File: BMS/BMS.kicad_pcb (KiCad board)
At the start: 2 copper layers, 53 parts, among them J1 Cell Taps, Q1 NSV1C201MZ4, Q2 BSS308PE, Q3 BSS308PE, Q4 BSS308PE, Q5 BSS308PE, Q6 BSS308PE, Q7 BSS308PE, Q8 BSS308PE, SW1 SW_DIP_x04, U1 LTC6811

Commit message: Updated BMS
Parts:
- added C12: 15pF, Capacitors_SMD:C_0805_HandSoldering, F.Cu at (390.8, 287.8)
- added C13: 1uF, Capacitors_SMD:C_0805_HandSoldering, F.Cu at (395.3, 287.8)
- added C14: 1uF, Capacitors_SMD:C_0805_HandSoldering, F.Cu at (390.8, 289.6)
- added J10: Current Sensor, Connectors_Molex:Molex_NanoFit_1x03x2.50mm_Straight, F.Cu at (368.5, 274.3)
- added J2: IsoSPI, Connectors_Molex:Molex_NanoFit_1x02x2.50mm_Straight, F.Cu at (368.5, 281.6)
- added J3: Temp 1, Connectors_Molex:Molex_NanoFit_1x02x2.50mm_Straight, F.Cu at (378.7, 274.3)
- added J4: Temp 2, Connectors_Molex:Molex_NanoFit_1x02x2.50mm_Straight, F.Cu at (368.5, 289.0)
- added J5: Temp 3, Connectors_Molex:Molex_NanoFit_1x02x2.50mm_Straight, F.Cu at (376.1, 281.6)
- added J6: Temp 4, Connectors_Molex:Molex_NanoFit_1x02x2.50mm_Straight, F.Cu at (386.3, 274.3)
- added J7: Temp 5, Connectors_Molex:Molex_NanoFit_1x02x2.50mm_Straight, F.Cu at (376.1, 289.0)
- added J8: Temp 6, Connectors_Molex:Molex_NanoFit_1x02x2.50mm_Straight, F.Cu at (383.8, 281.6)
- added J9: Temp 7, Connectors_Molex:Molex_NanoFit_1x02x2.50mm_Straight, F.Cu at (383.8, 289.0)
- added L1: HM2113ZNL, FSFootprints:HM2113ZNL, F.Cu at (361.1, 280.1)
- added R32: 402, Resistors_SMD:R_0805_HandSoldering, F.Cu at (358.9, 291.0)
- added R33: R, Resistors_SMD:R_0805_HandSoldering, F.Cu at (358.9, 292.9)
- added R34: R, Resistors_SMD:R_0805_HandSoldering, F.Cu at (393.4, 272.9)
- added R35: R, Resistors_SMD:R_0805_HandSoldering, F.Cu at (393.4, 274.8)
- added R36: R, Resistors_SMD:R_0805_HandSoldering, F.Cu at (393.4, 276.7)
- added R37: R, Resistors_SMD:R_0805_HandSoldering, F.Cu at (390.9, 280.3)
- added R38: R, Resistors_SMD:R_0805_HandSoldering, F.Cu at (390.9, 282.2)
- added R39: R, Resistors_SMD:R_0805_HandSoldering, F.Cu at (390.9, 284.1)
- added R40: 22, Resistors_SMD:R_0805_HandSoldering, F.Cu at (390.9, 286.0)
- added R41: 22, Resistors_SMD:R_0805_HandSoldering, F.Cu at (358.9, 289.1)
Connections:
- net Net-(R12-Pad1) renamed ICMP
- net Net-(R12-Pad2) renamed IBIAS
- U1 pad 32: (no net) -> Net-(J10-Pad2)
- U1 pad 41: (no net) -> IMA
- U1 pad 42: (no net) -> IPA

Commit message: Begin work on BMS schematic
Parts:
- C1, C11, C13, C14, C3, Q1, R12, R17, R2, R5, R6, R7, R8: moved to B.Cu
- J1: value Cell Taps -> Molex_Nano-Fit_105309-xx08_1x08_P2.50mm_Vertical; footprint FSFootprints:Cell Taps -> Connector_Molex:Molex_Nano-Fit_105309-xx08_1x08_P2.50mm_Vertical
- moved R30 244.7 mm to (273.9, 305.0), turned to 0 degrees
- moved Q8 227.4 mm to (283.5, 305.0), turned to 180 degrees
- moved R31 207.4 mm to (322.1, 292.1), turned to 0 degrees
- moved Q2 200.6 mm to (283.5, 275.0), turned to 180 degrees
- moved C6 184.7 mm to (347.8, 288.5), turned to 180 degrees
- moved R9 182.6 mm to (273.9, 275.0), turned to 0 degrees
- moved R27 181.2 mm to (273.9, 300.0), turned to 0 degrees
- moved Q3 168.7 mm to (283.5, 280.0), turned to 180 degrees
- moved Q7 165.2 mm to (283.5, 300.0), turned to 180 degrees
- moved R14 151.8 mm to (273.9, 280.0), turned to 0 degrees
- moved Q4 130.1 mm to (283.5, 285.0), turned to 180 degrees
- moved R24 124.9 mm to (273.9, 295.0), turned to 0 degrees
- moved R23 115.5 mm to (289.9, 296.0)
- moved Q6 113.2 mm to (283.5, 295.0), turned to 180 degrees
- moved J10 111.0 mm to (261.5, 303.8), turned to 270 degrees
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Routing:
- net V-: track 0.00 -> 57.8 mm
- net Net-(J1-Pad1): track 0.00 -> 40.6 mm
- net Net-(J1-Pad2): track 0.00 -> 32.9 mm
- net Net-(J1-Pad7): track 0.00 -> 31.8 mm
- net Net-(J1-Pad3): track 0.00 -> 31.8 mm
- net Net-(J1-Pad6): track 0.00 -> 30.8 mm
- net Net-(J1-Pad4): track 0.00 -> 30.6 mm
- net Net-(R29-Pad1): track 0.00 -> 30.1 mm
- net Net-(J1-Pad5): track 0.00 -> 29.8 mm
- net Net-(C2-Pad1): track 0.00 -> 25.7 mm
- net Net-(C10-Pad2): track 0.00 -> 24.0 mm, vias 0 -> 1
- net Net-(C5-Pad2): track 0.00 -> 23.9 mm
- net Net-(C2-Pad2): track 0.00 -> 21.3 mm
- net Net-(C10-Pad1): track 0.00 -> 20.3 mm
- net Net-(C4-Pad2): track 0.00 -> 19.5 mm
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
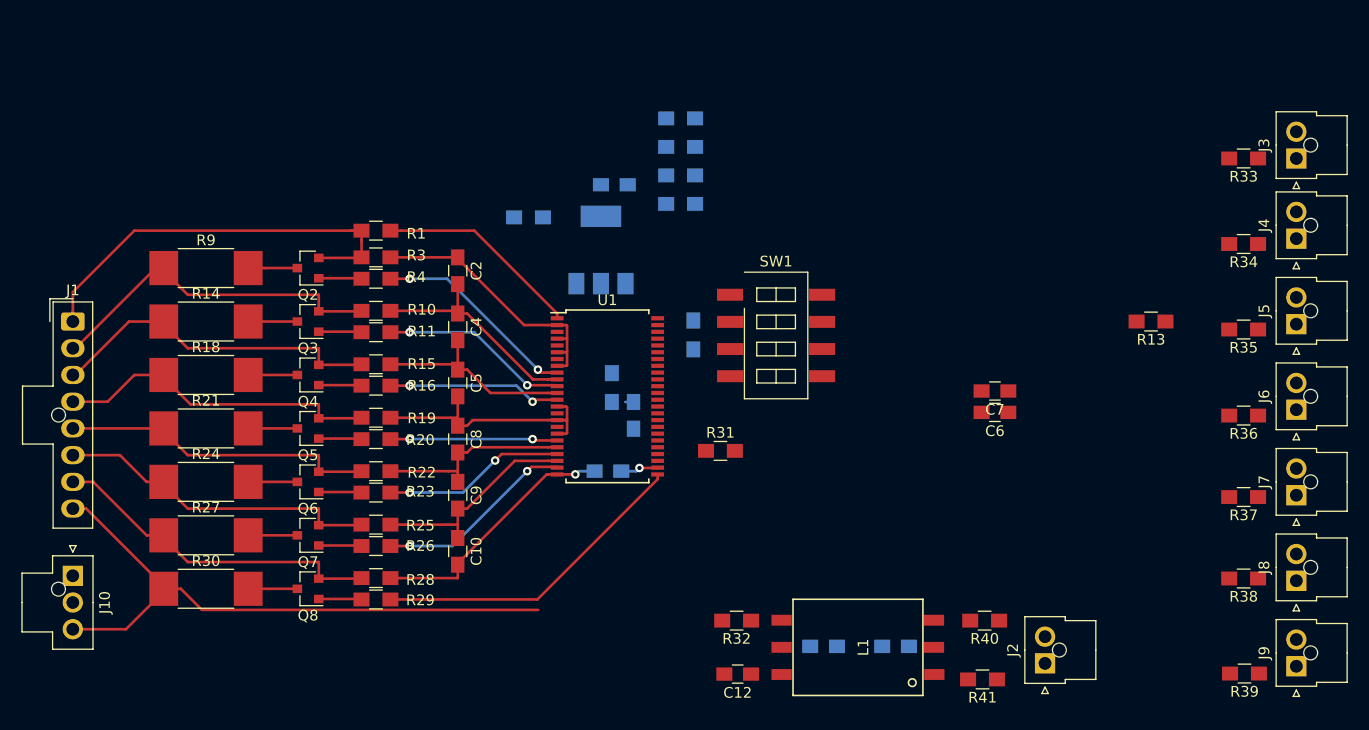
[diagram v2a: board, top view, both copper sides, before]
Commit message: BMS board v0.1
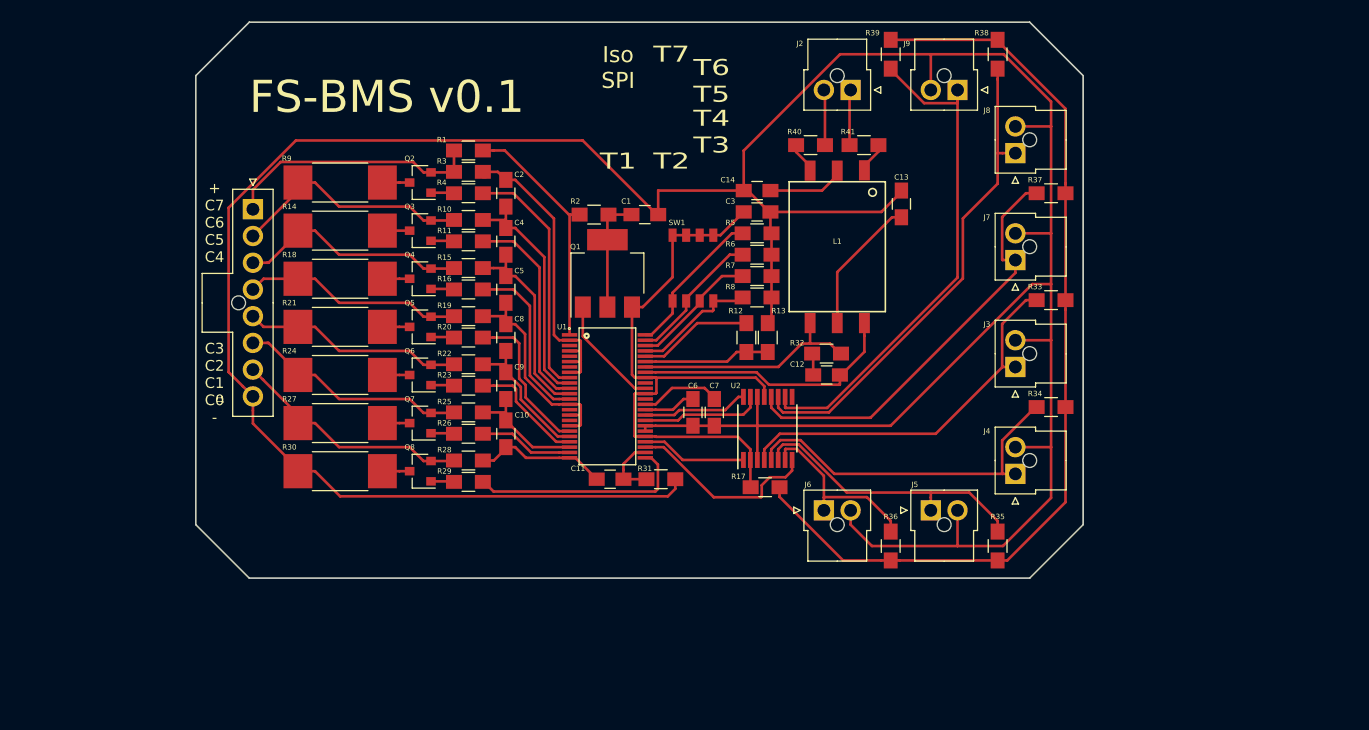
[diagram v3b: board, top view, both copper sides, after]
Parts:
- removed J10: Current Sensor, Connectors_Molex:Molex_NanoFit_1x03x2.50mm_Straight
- added U2: ADG708, Housings_SSOP:TSSOP-16_4.4x5mm_Pitch0.65mm, F.Cu at (326.5, 290.0)
- C1, C11, C3, Q1, R12, R2, R5, R6, R7, R8: moved to F.Cu
- C13, C14: value 1uF -> 10nF; moved to F.Cu
- J1: value Molex_Nano-Fit_105309-xx08_1x08_P2.50mm_Vertical -> Cell Taps; footprint Connector_Molex:Molex_Nano-Fit_105309-xx08_1x08_P2.50mm_Vertical -> Connectors_Molex:Molex_NanoFit_1x08x2.50mm_Straight
- R17: value 1M -> 0; moved to F.Cu
- R33, R34, R35, R36, R37, R38, R39: value R -> 10k
- SW1: footprint Buttons_Switches_SMD:SW_DIP_x4_W8.61mm_Slide_LowProfile -> FSFootprints:DIP A6H-4101
- U1: footprint Housings_SSOP:SSOP-48_7.5x15.9mm_Pitch0.635mm -> FSFootprints:FSOP-48_[LTC6811-2]
- moved R39 66.7 mm to (338.0, 255.0), turned to 90 degrees
- moved J9 62.5 mm to (344.2, 258.3), turned to 180 degrees
- moved J2 56.6 mm to (334.2, 258.3), turned to 180 degrees
- moved R38 54.2 mm to (348.0, 255.0), turned to 90 degrees
- moved R41 51.2 mm to (335.5, 263.5), turned to 0 degrees
- moved J8 47.9 mm to (349.7, 264.2)
- moved R40 47.4 mm to (330.5, 263.5)
- moved J6 45.2 mm to (331.8, 297.7), turned to 0 degrees
- moved C14 44.6 mm to (325.5, 267.8), turned to 180 degrees
- moved C13 42.0 mm to (339.0, 269.0), turned to 90 degrees
- moved J5 38.4 mm to (341.8, 297.7), turned to 0 degrees
- moved L1 37.5 mm to (333.0, 273.0), turned to 180 degrees
- moved R13 35.9 mm to (326.5, 281.5), turned to 270 degrees
- moved R36 35.2 mm to (338.0, 301.0), turned to 270 degrees
- moved J4 34.3 mm to (349.7, 294.2)
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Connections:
- R17 pad 2: Net-(R17-Pad2) -> VREG
- U1 pad 27: (no net) -> TEMP
- U1 pad 28: (no net) -> MUX_A0
- U1 pad 29: (no net) -> VREG
- U1 pad 32: Net-(J10-Pad2) -> MUX_A2
- U1 pad 33: (no net) -> MUX_A1
- U1 pad 39: Net-(R17-Pad2) -> (no net)
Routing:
- net V-: track 57.8 -> 315.6 mm
- net VREG: track 0.51 -> 148.2 mm
- net Net-(J9-Pad1): track 0.00 -> 48.6 mm
- net Net-(J8-Pad1): track 0.00 -> 46.3 mm
- net Net-(J7-Pad1): track 0.00 -> 40.4 mm
- net Net-(J3-Pad1): track 0.00 -> 35.9 mm
- net Net-(J4-Pad1): track 0.00 -> 33.2 mm
- net Net-(J5-Pad1): track 0.00 -> 27.3 mm
- net IMA: track 0.00 -> 25.5 mm
- net IPA: track 0.00 -> 21.5 mm
- net TEMP: track 0.00 -> 18.3 mm
- net Net-(J6-Pad1): track 0.00 -> 17.1 mm
- net Net-(J1-Pad1): track 40.6 -> 24.1 mm
- net A3: track 0.00 -> 14.2 mm
- net A2: track 0.00 -> 13.1 mm
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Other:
- board outline added: 83 x 52 mm
- net class Default: clearance 0.2 -> 0.16
- rule trace_clearance: 0.2 -> 0.16
- board text added: "+ C7 C6 C5 C4"
- board text added: "C3 C2 C1 C0 -"
- board text added: "FS-BMS v0.1"
- board text added: "Iso SPI"
- board text added: "T1"
- board text added: "T2"
- board text added: "T3"
- board text added: "T4"
- board text added: "T5"
- board text added: "T6"
- board text added: "T7"

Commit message: yikes
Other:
- net class Default: clearance 0.16 -> 0.1778
- rule trace_clearance: 0.16 -> 0.1778
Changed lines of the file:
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@@
     (34 B.Paste user hide)
     (35 F.Paste user hide)
-    (36 B.SilkS user)
+    (36 B.SilkS user hide)
     (37 F.SilkS user)
     (38 B.Mask user)
-    (39 F.Mask user)
+    (39 F.Mask user hide)
     (40 Dwgs.User user)
     (41 Cmts.User user)
@@
   (setup
     (last_trace_width 0.25)
-    (trace_clearance 0.16)
+    (trace_clearance 0.1778)
     (zone_clearance 0.508)
     (zone_45_only no)
@@
   (net 69 MUX_A0)
   (net_class Default "This is the default net class."
-    (clearance 0.16)
+    (clearance 0.1778)
     (trace_width 0.25)
     (via_dia 0.8)

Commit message: Began BMS slave board
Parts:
- removed C14: 10nF, Capacitors_SMD:C_0805_HandSoldering
- added D1: LH R974-LP-1, LEDs:LED_0805_HandSoldering, F.Cu at (107.2, 206.5)
- added D2: LH R974-LP-1, LEDs:LED_0805_HandSoldering, F.Cu at (367.2, 266.4)
- added D3: LH R974-LP-1, LEDs:LED_0805_HandSoldering, F.Cu at (372.9, 263.5)
- added D4: LH R974-LP-1, LEDs:LED_0805_HandSoldering, F.Cu at (367.2, 269.2)
- added D5: LH R974-LP-1, LEDs:LED_0805_HandSoldering, F.Cu at (372.9, 266.4)
- added D6: LH R974-LP-1, LEDs:LED_0805_HandSoldering, F.Cu at (367.2, 272.1)
- added D7: LH R974-LP-1, LEDs:LED_0805_HandSoldering, F.Cu at (378.7, 263.5)
- added D8: LH R974-LP-1, LEDs:LED_0805_HandSoldering, F.Cu at (367.2, 274.9)
- added D9: LH R974-LP-1, LEDs:LED_0805_HandSoldering, F.Cu at (321.0, 218.5)
- added R42: 120, Resistors_SMD:R_0805_HandSoldering, F.Cu at (342.5, 204.5)
- added R43: 2.2k, Resistors_SMD:R_0805_HandSoldering, F.Cu at (390.2, 263.5)
- added R44: 2.2k, Resistors_SMD:R_0805_HandSoldering, F.Cu at (378.7, 275.0)
- added R45: 2.2k, Resistors_SMD:R_0805_HandSoldering, F.Cu at (384.4, 269.3)
- added R46: 2.2k, Resistors_SMD:R_0805_HandSoldering, F.Cu at (390.2, 266.4)
- added R47: 2.2k, Resistors_SMD:R_0805_HandSoldering, F.Cu at (378.7, 277.9)
- added R48: 2.2k, Resistors_SMD:R_0805_HandSoldering, F.Cu at (384.4, 272.2)
- added R49: 120, Resistors_SMD:R_0805_HandSoldering, F.Cu at (390.2, 269.3)
- added R50: 120, Resistors_SMD:R_0805_HandSoldering, F.Cu at (384.4, 275.0)
- added R51: 160, Resistors_SMD:R_0805_HandSoldering, F.Cu at (321.0, 221.4)
- J1: footprint Connectors_Molex:Molex_NanoFit_1x08x2.50mm_Straight -> FSFootprints:Cell Taps
- R12: value R -> 1.5k
- R13: value R -> 680
- R17: value 0 -> 120
- R33: value 10k -> 2.2k
- R34, R35, R36: value 10k -> 120
- R5: value 10k -> 200
- R6: value 10k -> 160
- moved J3 274.6 mm to (91.2, 191.3), turned to 180 degrees
- moved R30 223.7 mm to (489.5, 200.0), turned to 180 degrees
- moved J4 214.7 mm to (161.2, 191.3), turned to 180 degrees
- moved Q8 210.2 mm to (482.0, 200.0), turned to 0 degrees
- moved R3 201.1 mm to (107.2, 203.8)
- moved C2 200.6 mm to (112.0, 203.8), turned to 0 degrees
- moved Q2 198.6 mm to (107.0, 200.0), turned to 0 degrees
- moved J2 192.8 mm to (150.8, 198.8), turned to 270 degrees
- moved R41 192.4 mm to (155.0, 197.0), turned to 270 degrees
- moved R40 185.6 mm to (155.0, 203.0), turned to 270 degrees
- moved R9 184.6 mm to (114.5, 200.0), turned to 180 degrees
- moved L1 183.2 mm to (165.0, 200.0), turned to 270 degrees
- moved J9 179.9 mm to (511.2, 191.3)
- moved R27 160.3 mm to (419.5, 200.0), turned to 180 degrees
- moved J5 153.3 mm to (231.2, 191.3), turned to 180 degrees
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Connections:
- C1 pad 1: Net-(C1-Pad1) -> V+OUT
- L1 pad 2: Net-(C14-Pad1) -> (no net)
- Q1 pad 2: Net-(C1-Pad1) -> V+OUT
- Q1 pad 4: Net-(C1-Pad1) -> V+OUT
- R17 pad 1: VREG -> Net-(Q2-Pad3)
- R17 pad 2: VREG -> Net-(D2-Pad2)
- R2 pad 1: Net-(C1-Pad1) -> V+IN
- R34 pad 1: Net-(J4-Pad1) -> Net-(Q3-Pad3)
- R34 pad 2: VREG -> Net-(D3-Pad2)
- R35 pad 1: Net-(J5-Pad1) -> Net-(Q4-Pad3)
- R35 pad 2: VREG -> Net-(D4-Pad2)
- R36 pad 1: Net-(J6-Pad1) -> Net-(Q5-Pad3)
- R36 pad 2: VREG -> Net-(D5-Pad2)
- R37 pad 1: Net-(J7-Pad1) -> MUX_A0
- R38 pad 1: Net-(J8-Pad1) -> MUX_A1
- R39 pad 1: Net-(J9-Pad1) -> MUX_A2
- R5 pad 1: A3 -> Net-(R5-Pad1)
- R5 pad 2: V- -> IPA
- R6 pad 1: A2 -> Net-(D1-Pad2)
- R6 pad 2: V- -> VREG
- SW1 pad 1: A3 -> V+IN
- SW1 pad 2: A2 -> Net-(R5-Pad1)
- SW1 pad 7: VREG -> IMA
- SW1 pad 8: VREG -> V+OUT
- U1 pad 27: TEMP -> MUX_A0
- U1 pad 28: MUX_A0 -> MUX_A1
- U1 pad 29: VREG -> MUX_A2
- U1 pad 32: MUX_A2 -> TEMP
- U1 pad 33: MUX_A1 -> (no net)
- U1 pad 47: A2 -> V-
- U1 pad 48: A3 -> V-
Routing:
- net V-: track 315.6 -> 0.00 mm
- net VREG: track 148.2 -> 0.00 mm
- net Net-(J9-Pad1): track 48.6 -> 0.00 mm
- net Net-(J8-Pad1): track 46.3 -> 0.00 mm
- net Net-(J7-Pad1): track 40.4 -> 0.00 mm
- net Net-(J3-Pad1): track 35.9 -> 0.00 mm
- net Net-(J4-Pad1): track 33.2 -> 0.00 mm
- net Net-(J5-Pad1): track 27.3 -> 0.00 mm
- net IMA: track 25.5 -> 0.00 mm
- net Net-(J1-Pad1): track 24.1 -> 0.00 mm
- net Net-(R4-Pad1): track 22.9 -> 0.00 mm
- net Net-(D7-Pad1): track 22.8 -> 0.00 mm
- net Net-(D2-Pad1): track 22.8 -> 0.00 mm
- net Net-(C2-Pad2): track 22.3 -> 0.00 mm
- net Net-(D6-Pad1): track 21.7 -> 0.00 mm
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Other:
- board outline removed
- board text removed: "+ C7 C6 C5 C4"
- board text removed: "C3 C2 C1 C0 -"
- board text removed: "FS-BMS v0.1"
- board text removed: "Iso SPI"
- board text removed: "T1"
- board text removed: "T2"
- board text removed: "T3"
- board text removed: "T4"
- board text removed: "T5"
- board text removed: "T6"
- board text removed: "T7"

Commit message: fixed shit
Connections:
- U1 pad 33: (no net) -> Net-(D9-Pad1)
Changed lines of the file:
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@@
     (pad 32 smd rect (at 3.54 2.25 90) (size 1.44 0.34) (layers F.Cu F.Paste F.Mask)
       (net 56 TEMP))
-    (pad 33 smd rect (at 3.54 1.75 90) (size 1.44 0.34) (layers F.Cu F.Paste F.Mask))
+    (pad 33 smd rect (at 3.54 1.75 90) (size 1.44 0.34) (layers F.Cu F.Paste F.Mask)
+      (net 77 "Net-(D9-Pad1)"))
     (pad 34 smd rect (at 3.54 1.25 90) (size 1.44 0.34) (layers F.Cu F.Paste F.Mask)
       (net 7 "Net-(C6-Pad2)"))

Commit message: BMS update pre-autorouter
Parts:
- removed R31: 100, Resistors_SMD:R_0805_HandSoldering
- removed R43, R44, R45, R46, R47, R48: 2.2k, Resistors_SMD:R_0805_HandSoldering
- added J10: IsoSPI, Connectors_Molex:Molex_NanoFit_1x02x2.50mm_Straight, F.Cu at (476.2, 192.3)
- moved R17 290.4 mm to (90.0, 206.5)
- moved D2 283.1 mm to (90.0, 208.5)
- moved D3 219.9 mm to (160.0, 208.5)
- moved R34 219.1 mm to (160.0, 206.5)
- moved R29 211.1 mm to (485.5, 197.0)
- moved R4 210.3 mm to (100.5, 197.0)
- moved R28 207.5 mm to (485.5, 203.0)
- moved C11 200.9 mm to (490.5, 203.0)
- moved R40 196.1 mm to (351.0, 207.5), turned to 180 degrees
- moved R1 193.8 mm to (100.5, 205.0), turned to 180 degrees
- moved R41 184.3 mm to (339.0, 207.5), turned to 0 degrees
- moved L1 180.0 mm to (345.0, 200.0), turned to 0 degrees
- moved D1 176.3 mm to (283.5, 208.5), turned to 180 degrees
- moved R26 169.6 mm to (440.0, 197.0)
- moved C10 167.6 mm to (445.0, 203.0), turned to 0 degrees
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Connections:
- net Net-(C10-Pad1) renamed /C2
- net Net-(C10-Pad2) renamed /C1
- net Net-(C2-Pad1) renamed /C9-12
- net Net-(C2-Pad2) renamed /C8
- net Net-(C4-Pad2) renamed /C7
- net Net-(C5-Pad2) renamed /C4-6
- net Net-(C8-Pad2) renamed /C3
- net Net-(Q1-Pad1) renamed /DRV
- net Net-(R1-Pad1) renamed /V+
- net Net-(R11-Pad1) renamed /S8
- net Net-(R16-Pad1) renamed /S7
- net Net-(R20-Pad1) renamed /S4
- net Net-(R23-Pad1) renamed /S3
- net Net-(R26-Pad1) renamed /S2
- net Net-(R29-Pad1) renamed /S1
- net Net-(R4-Pad1) renamed /S9
- C11 pad 2: Net-(C11-Pad2) -> V-
- R33 pad 1: Net-(J3-Pad1) -> TEMP
- U1 pad 26: Net-(C11-Pad2) -> V-
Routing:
- net Net-(D6-Pad1): track 0.00 -> 60.1 mm
- net Net-(D3-Pad1): track 6.55 -> 60.1 mm
- net Net-(D5-Pad1): track 6.55 -> 60.1 mm
- net Net-(D4-Pad1): track 6.55 -> 60.1 mm
- net Net-(D2-Pad1): track 0.00 -> 49.6 mm
- net Net-(D7-Pad1): track 0.00 -> 35.6 mm
- net V-: track 0.00 -> 34.7 mm
- net Net-(J1-Pad1): track 0.00 -> 13.5 mm
- net ICMP: track 0.00 -> 3.53 mm
- net V+IN: track 0.00 -> 3.31 mm
- net Net-(Q8-Pad3): track 0.00 -> 2.55 mm
- net Net-(Q7-Pad3): track 0.00 -> 2.55 mm
- net Net-(Q6-Pad3): track 0.00 -> 2.50 mm
- net /C9-12: track 7.01 -> 9.41 mm
- net /C8: track 0.00 -> 2.40 mm
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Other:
- board outline added: 428 x 20 mm

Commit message: BMS pcb routed
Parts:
- moved C6 1.12 mm to (293.0, 191.8)
- moved C7 1.12 mm to (291.0, 191.8)
- moved R12 1.12 mm to (287.0, 191.8)
- moved R13 1.12 mm to (289.0, 191.8)
- moved R7 1.12 mm to (283.0, 191.8)
- moved R8 1.12 mm to (285.0, 191.8)
- moved D1 0.50 mm to (284.0, 208.5)
- moved D9 0.50 mm to (292.0, 208.5)
- moved R51 0.50 mm to (292.0, 206.5)
- moved R6 0.50 mm to (284.0, 206.5)
- moved U1 0.50 mm to (288.0, 200.0)
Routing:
- net V-: track 34.7 -> 593.0 mm, vias 0 -> 2
- net Net-(J10-Pad1): track 0.00 -> 367.3 mm, vias 0 -> 1
- net Net-(J10-Pad2): track 0.00 -> 365.8 mm, vias 0 -> 1
- net Net-(J3-Pad1): track 0.00 -> 230.4 mm, vias 0 -> 1
- net Net-(J9-Pad1): track 0.00 -> 205.8 mm, vias 0 -> 1
- net /C1: track 2.40 -> 203.0 mm, vias 0 -> 2
- net /S1: track 0.00 -> 199.1 mm
- net /C9-12: track 9.41 -> 202.0 mm
- net /S9: track 0.00 -> 189.3 mm, vias 0 -> 2
- net /C8: track 2.40 -> 189.5 mm, vias 0 -> 2
- net /V+: track 3.79 -> 187.8 mm
- net Net-(J4-Pad1): track 0.00 -> 173.1 mm
- net /C2: track 2.40 -> 156.1 mm, vias 0 -> 2
- net /S2: track 0.00 -> 153.2 mm, vias 0 -> 2
- net VREG: track 1.27 -> 149.1 mm, vias 0 -> 4
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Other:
- board size 428 x 20 mm -> 428 x 25 mm
